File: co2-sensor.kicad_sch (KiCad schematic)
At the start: 51 parts, among them J1 24-pin FPC Connector, J2 USB-C Receptacle, J3 JST 2-PH, Q1 AO3401A, Q2 AO3400A, SW1 SW_Push, SW2 SW_Push, SW3 SW_Push, SW4 SW_Push, SW5 SW_Push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

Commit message: Add labels and OSHW logo
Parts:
- added H1, H2, H3: MountingHole, MountingHole:MountingHole_2.2mm_M2, symbol Mechanical:MountingHole
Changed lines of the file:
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@@
 	(label "BTN2"
 		(at 143.51 128.27 0)
-		(fields_autoplaced yes)
 		(effects
 			(font
@@
 	(label "EINK_RES"
 		(at 176.53 73.66 0)
-		(fields_autoplaced yes)
 		(effects
 			(font
@@
 	(label "RESE"
 		(at 246.38 66.04 0)
-		(fields_autoplaced yes)
 		(effects
 			(font
@@
 	(label "BTN3"
 		(at 161.29 128.27 0)
-		(fields_autoplaced yes)
 		(effects
 			(font
@@
 	(label "I2C_SCL"
 		(at 110.49 73.66 180)
-		(fields_autoplaced yes)
 		(effects
 			(font
@@
 	(label "BTN1"
 		(at 110.49 50.8 180)
-		(fields_autoplaced yes)
 		(effects
 			(font
@@
 	(label "EINK_SCLK"
 		(at 254 115.57 180)
-		(fields_autoplaced yes)
 		(effects
 			(font
@@
 	(label "EN"
 		(at 110.49 45.72 180)
-		(fields_autoplaced yes)
 		(effects
 			(font
@@
 	(label "EINK_SCLK"
 		(at 176.53 81.28 0)
-		(fields_autoplaced yes)
 		(effects
 			(font
@@
 	(label "BTN1"
 		(at 127 128.27 0)
-		(fields_autoplaced yes)
 		(effects
 			(font
@@
 	(label "EINK_CS"
 		(at 176.53 78.74 0)
-		(fields_autoplaced yes)
 		(effects
 			(font
@@
 	(label "D-"
 		(at 176.53 55.88 0)
-		(fields_autoplaced yes)
 		(effects
 			(font
@@
 	(label "EINK_DC"
 		(at 254 110.49 180)
-		(fields_autoplaced yes)
 		(effects
 			(font
@@
 	(label "EINK_BUSY"
 		(at 110.49 58.42 180)
-		(fields_autoplaced yes)
 		(effects
 			(font
@@
 	(label "CO2_NRDY"
 		(at 149.86 186.69 0)
-		(fields_autoplaced yes)
 		(effects
 			(font
@@
 	(label "GDR"
 		(at 236.22 66.04 0)
-		(fields_autoplaced yes)
 		(effects
 			(font
@@
 	(label "CO2_EN"
 		(at 111.76 189.23 180)
-		(fields_autoplaced yes)
 		(effects
 			(font
@@
 	(label "I2C_SDA"
 		(at 57.15 189.23 0)
-		(fields_autoplaced yes)
 		(effects
 			(font
@@
 	(label "PREVGH"
 		(at 269.24 49.53 0)
-		(fields_autoplaced yes)
 		(effects
 			(font
@@
 	(label "EINK_DC"
 		(at 176.53 76.2 0)
-		(fields_autoplaced yes)
 		(effects
 			(font
@@
 	(label "I2C_SCL"
 		(at 111.76 181.61 180)
-		(fields_autoplaced yes)
 		(effects
 			(font
@@
 	(label "GDR"
 		(at 251.46 87.63 180)
-		(fields_autoplaced yes)
 		(effects
 			(font
@@
 	(label "RESE"
 		(at 251.46 90.17 180)
-		(fields_autoplaced yes)
 		(effects
 			(font
@@
 	(label "EINK_MOSI"
 		(at 176.53 83.82 0)
-		(fields_autoplaced yes)
 		(effects
 			(font
@@
 	(label "BOOT9"
 		(at 176.53 68.58 0)
-		(fields_autoplaced yes)
 		(effects
 			(font
@@
 	(label "VCOM"
 		(at 248.92 143.51 0)
-		(fields_autoplaced yes)
 		(effects
 			(font
@@
 	(label "CO2_NRDY"
 		(at 110.49 68.58 180)
-		(fields_autoplaced yes)
 		(effects
 			(font
@@
 	(label "EINK_BUSY"
 		(at 254 105.41 180)
-		(fields_autoplaced yes)
 		(effects
 			(font
@@
 	(label "I2C_SDA"
 		(at 111.76 179.07 180)
-		(fields_autoplaced yes)
 		(effects
 			(font
@@
 	(label "BTN3"
 		(at 110.49 55.88 180)
-		(fields_autoplaced yes)
 		(effects
 			(font
@@
 	(label "EINK_MOSI"
 		(at 254 118.11 180)
-		(fields_autoplaced yes)
 		(effects
 			(font
@@
 	(label "BOOT8"
 		(at 176.53 66.04 0)
-		(fields_autoplaced yes)
 		(effects
 			(font
@@
 	(label "D+"
 		(at 48.26 46.99 0)
-		(fields_autoplaced yes)
 		(effects
 			(font
@@
 	(label "D-"
 		(at 48.26 41.91 0)
-		(fields_autoplaced yes)
 		(effects
 			(font
@@
 	(label "PREVGL"
 		(at 254 140.97 180)
-		(fields_autoplaced yes)
 		(effects
 			(font
@@
 	(label "I2C_SCL"
 		(at 57.15 186.69 0)
-		(fields_autoplaced yes)
 		(effects
 			(font
@@
 	(label "BTN2"
 		(at 110.49 53.34 180)
-		(fields_autoplaced yes)
 		(effects
 			(font
@@
 	(label "EINK_CS"
 		(at 254 113.03 180)
-		(fields_autoplaced yes)
 		(effects
 			(font
@@
 	(label "PREVGL"
 		(at 270.51 24.13 0)
-		(fields_autoplaced yes)
 		(effects
 			(font
@@
 	(label "CO2_EN"
 		(at 110.49 66.04 180)
-		(fields_autoplaced yes)
 		(effects
 			(font
@@
 	(label "I2C_SDA"
 		(at 110.49 71.12 180)
-		(fields_autoplaced yes)
 		(effects
 			(font
@@
 	(label "D+"
 		(at 176.53 53.34 0)
-		(fields_autoplaced yes)
 		(effects
 			(font
@@
 	(label "EINK_RES"
 		(at 254 107.95 180)
-		(fields_autoplaced yes)
 		(effects
 			(font
@@
 	(label "PREVGH"
 		(at 254 135.89 180)
-		(fields_autoplaced yes)
 		(effects
 			(font
@@
 	)
 	(symbol
+		(lib_id "Mechanical:MountingHole")
+		(at 190.5 133.35 0)
+		(unit 1)
+		(exclude_from_sim yes)
+		(in_bom no)
+		(on_board yes)
+		(dnp no)
+		(fields_autoplaced yes)
+		(property "Reference" "H2"
+			(at 193.04 132.0799 0)
+			(effects
+				(font
+					(size 1.27 1.27)
+				)
+				(justify left)
+			)
+		)
+		(property "Value" "MountingHole"
+			(at 193.04 134.6199 0)
+			(effects
+				(font
+					(size 1.27 1.27)
+				)
+				(justify left)
+			)
+		)
+		(property "Footprint" "MountingHole:MountingHole_2.2mm_M2"
+			(at 190.5 133.35 0)
+			(effects
+				(font
+					(size 1.27 1.27)
+				)
+				(hide yes)
+			)
+		)
+		(property "Datasheet" "~"
+			(at 190.5 133.35 0)
+			(effects
+				(font
+					(size 1.27 1.27)
+				)
+				(hide yes)
+			)
+		)
+		(property "Description" "Mounting Hole without connection"
+			(at 190.5 133.35 0)
+			(effects
+				(font
+					(size 1.27 1.27)
+				)
+				(hide yes)
+			)
+		)
+		(instances
+			(project "co2-sensor"
+				(path "/14a75f0f-668c-4fbd-ad64-ed80bbf70e47"
+					(reference "H2")
+					(unit 1)
+				)
+			)
+		)
+	)
+	(symbol
 		(lib_id "power:GND")
 		(at 143.51 100.33 0)
@@
 	)
 	(symbol
+		(lib_id "Mechanical:MountingHole")
+		(at 190.5 143.51 0)
+		(unit 1)
+		(exclude_from_sim yes)
+		(in_bom no)
+		(on_board yes)
+		(dnp no)
+		(fields_autoplaced yes)
+		(property "Reference" "H3"
+			(at 193.04 142.2399 0)
+			(effects
+				(font
+					(size 1.27 1.27)
+				)
+				(justify left)
+			)
+		)
+		(property "Value" "MountingHole"
+			(at 193.04 144.7799 0)
+			(effects
+				(font
+					(size 1.27 1.27)
+				)
+				(justify left)
+			)
+		)
+		(property "Footprint" "MountingHole:MountingHole_2.2mm_M2"
+			(at 190.5 143.51 0)
+			(effects
+				(font
+					(size 1.27 1.27)
+				)
+				(hide yes)
+			)
+		)
+		(property "Datasheet" "~"
+			(at 190.5 143.51 0)
+			(effects
+				(font
+					(size 1.27 1.27)
+				)
+				(hide yes)
+			)
+		)
+		(property "Description" "Mounting Hole without connection"
+			(at 190.5 143.51 0)
+			(effects
+				(font
+					(size 1.27 1.27)
+				)
+				(hide yes)
+			)
+		)
+		(instances
+			(project "co2-sensor"
+				(path "/14a75f0f-668c-4fbd-ad64-ed80bbf70e47"
+					(reference "H3")
+					(unit 1)
+				)
+			)
+		)
+	)
+	(symbol
 		(lib_id "power:+3.3V")
 		(at 240.03 118.11 0)
@@
 					(unit 1)
 				)
+			)
+		)
+	)
+	(symbol
+		(lib_id "Mechanical:MountingHole")
+		(at 190.5 123.19 0)
+		(unit 1)
+		(exclude_from_sim yes)
+		(in_bom no)
+		(on_board yes)
+		(dnp no)
+		(fields_autoplaced yes)
+		(property "Reference" "H1"
+			(at 193.04 121.9199 0)
+			(effects
+				(font
+					(size 1.27 1.27)
+				)
+				(justify left)
+			)
+		)
+		(property "Value" "MountingHole"
+			(at 193.04 124.4599 0)
+			(effects
+				(font
+					(size 1.27 1.27)
+				)
+				(justify left)
+			)
+		)
+		(property "Footprint" "MountingHole:MountingHole_2.2mm_M2"
+			(at 190.5 123.19 0)
+			(effects
+				(font
+					(size 1.27 1.27)
+				)
+				(hide yes)
+			)
+		)
+		(property "Datasheet" "~"
+			(at 190.5 123.19 0)
+			(effects
+				(font
+					(size 1.27 1.27)
+				)
+				(hide yes)
+			)
+		)
+		(property "Description" "Mounting Hole without connection"
+			(at 190.5 123.19 0)
+			(effects
+				(font
+					(size 1.27 1.27)
+				)
+				(hide yes)
+			)
+		)
+		(instances
+			(project ""
+				(path "/14a75f0f-668c-4fbd-ad64-ed80bbf70e47"
+					(reference "H1")
+					(unit 1)
+				)

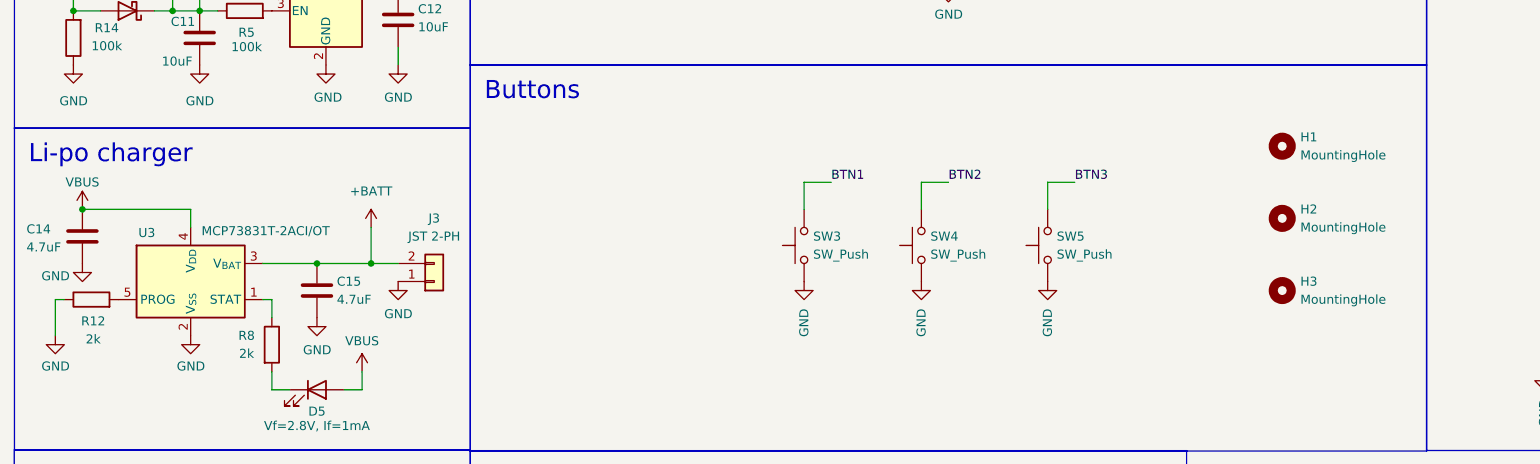
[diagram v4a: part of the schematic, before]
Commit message: Add pins for providing BAT power
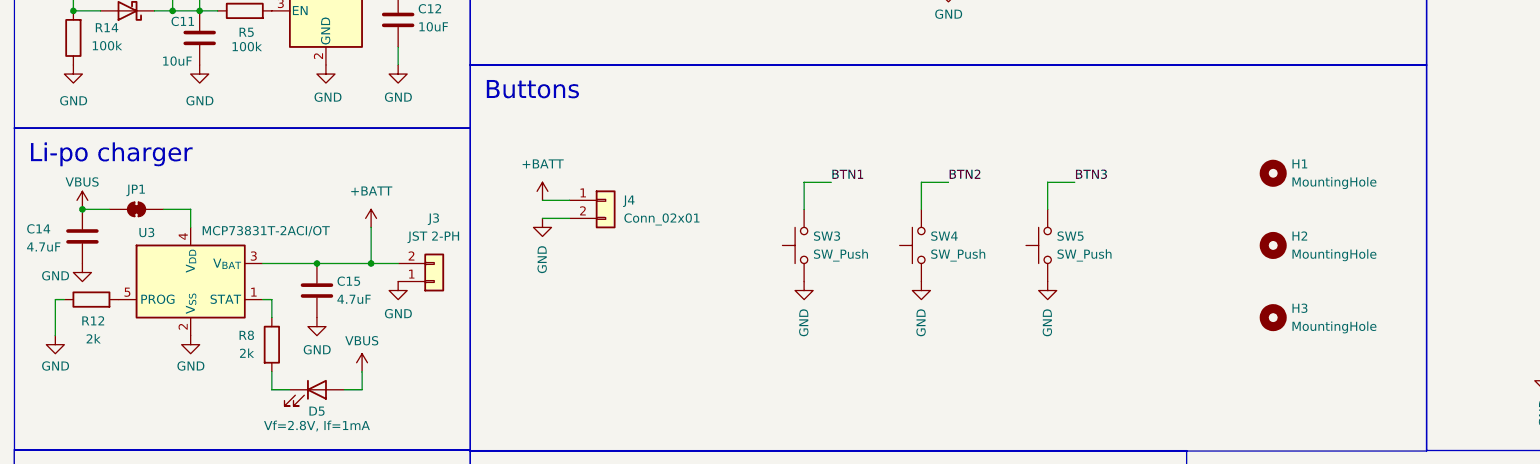
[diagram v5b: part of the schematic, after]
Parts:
- added J4: Conn_02x01, Connector_PinHeader_2.54mm:PinHeader_1x02_P2.54mm_Vertical, symbol Connector_Generic:Conn_01x02
- added JP1: SolderJumper_2_Bridged, symbol Jumper:SolderJumper_2_Bridged
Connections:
- net +BATT: now also J4.1 (Pin_1)
- net GND: now also J4.2 (Pin_2)
- net VBUS: now also JP1.1 (A); no longer U3.4 (V_{DD})
- new net: JP1.2 (B), U3.4 (V_{DD})
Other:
- moved on the sheet: H1, H2, H3

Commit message: Improve labels
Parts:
- J1: JLCPCB Position Offset 0,0.381 -> 0,0.6985
- J4: now left out of the parts list
- JP1: footprint (none) -> Jumper:SolderJumper-2_P1.3mm_Bridged_RoundedPad1.0x1.5mm
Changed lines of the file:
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@@
 		(unit 1)
 		(exclude_from_sim no)
-		(in_bom yes)
+		(in_bom no)
 		(on_board yes)
 		(dnp no)
@@
 			)
 		)
-		(property "Footprint" ""
+		(property "Footprint" "Jumper:SolderJumper-2_P1.3mm_Bridged_RoundedPad1.0x1.5mm"
 			(at 29.21 132.08 0)
 			(effects
@@
 			)
 		)
-		(property "JLCPCB Position Offset" "0,0.381"
+		(property "JLCPCB Position Offset" "0,0.6985"
 			(at 262.89 113.03 0)
 			(effects
